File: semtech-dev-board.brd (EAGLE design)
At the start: 74 x 66 mm, 73 parts, among them Q1 BSS123, U1 MIC5219 3.3V, U2 QUALCOMM-TDK_B3710, U3 QUALCOMM-TDK_B3588, U4 SEMTECH_SX1236, Y1 32MHz

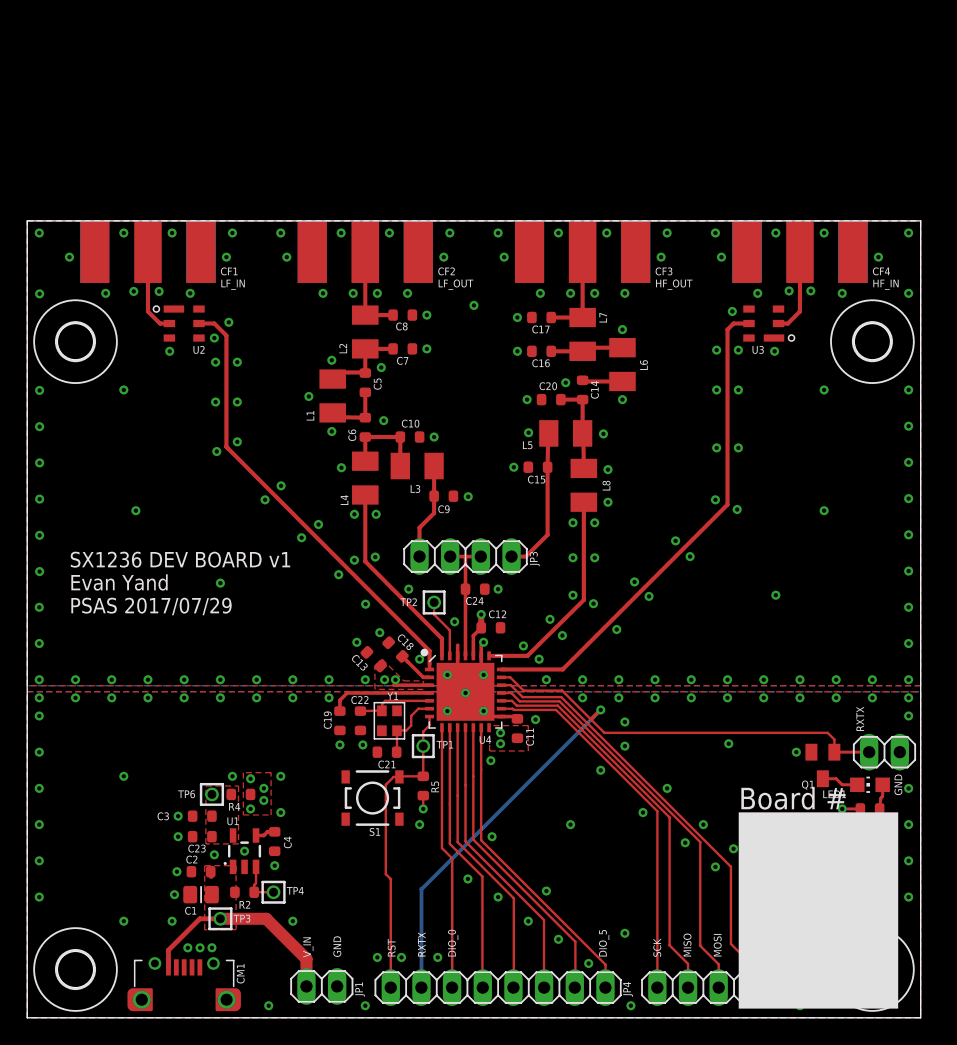
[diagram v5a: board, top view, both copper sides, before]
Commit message: Chose parts and added Digikey part numbers to BoM, switched inductors to 0603 because it was easy, shrunk board by 3 mm, cleaned up stapling, switched LEDs to 0603, oh and added a power LED for fun.
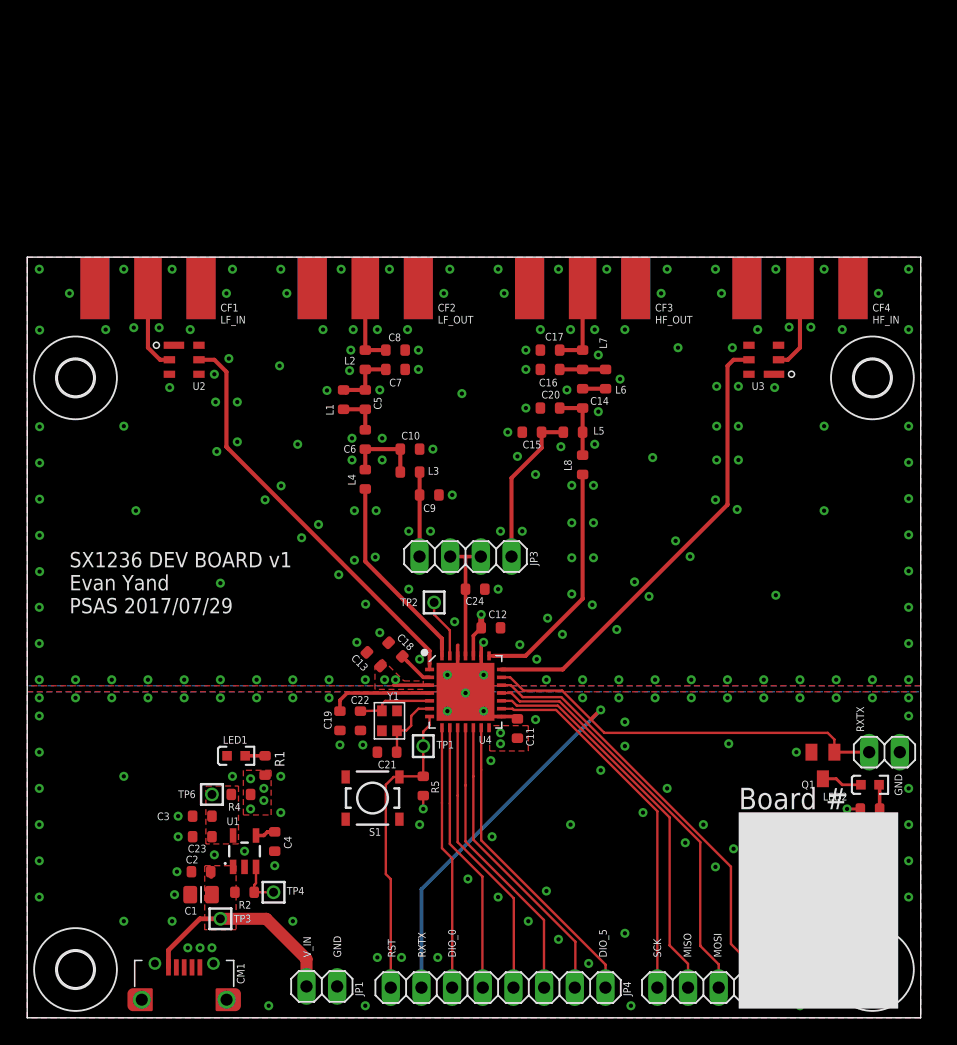
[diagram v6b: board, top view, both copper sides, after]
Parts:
- added LED2: AMB, low-gain-radio:LED-0603
- added R1: 1k, rcl_custom:.0603-B-NOSILK
- CM1: value (none) -> ZX62D-B-5P8(30)
- L1, L2, L3, L4, L5, L6, L7, L8: device rcl:L3225M -> rcl_custom:.0603-B-NOSILK
- LED1: value (none) -> GRN; device led:CHIP-LED0805 -> low-gain-radio:LED-0603
- Q1: value BSS123 -> DMN62D0U-13
- R2, R5: value 1k -> 10k
- S1: value SWITCH-MOMENTARY-2SMD-2 -> FSM4JSMATR
- moved LED1 52.6 mm to (17.3, 21.7), turned to 0 degrees
- moved CF1 3.00 mm to (10.0, 60.4)
- moved CF2 3.00 mm to (28.0, 60.4)
- moved CF3 3.00 mm to (46.0, 60.4)
- moved CF4 3.00 mm to (64.0, 60.4)
- moved U$12 3.00 mm to (72.0, 46.0)
- moved U$3 3.00 mm to (2.00, 46.0)
- moved U$8 3.00 mm to (4.00, 53.0)
- moved U$9 3.00 mm to (70.0, 53.0)
- moved U2 3.00 mm to (13.0, 54.5)
- moved U3 3.00 mm to (61.0, 54.5)
- moved C8 2.96 mm to (30.5, 55.3)
- moved C15 2.94 mm to (41.8, 48.5)
- moved C17 2.79 mm to (43.3, 55.3)
- moved L2 2.30 mm to (28.0, 54.5)
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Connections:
- new net N$5: LED1.A, R1.1
- net +3V3: now also R1.2
- net GND: now also LED1.K
- net LED+: now also LED2.A; no longer LED1.A
- net LED-: now also LED2.K; no longer LED1.C
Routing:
- net RFI_LF: track 37.5 -> 34.5 mm
- net RFI_HF: track 40.9 -> 37.9 mm
- net RFO_HF_2: track 6.02 -> 3.80 mm
- net RFO_HF: track 17.9 -> 20.0 mm
- net RFO_LF_2: track 7.26 -> 5.37 mm
- net RFO_HF_PA: track 7.66 -> 5.80 mm
- net N$5: track 0.00 -> 1.65 mm
- net RFO_LF_1: track 4.98 -> 3.50 mm
- net RFO_HF_1: track 3.32 -> 1.90 mm
- net LFO_PA_HEAD: track 8.08 -> 7.00 mm
- net RFO_HF_OUT: track 8.00 -> 7.00 mm
- net HFO_PA_HEAD: track 12.3 -> 13.1 mm
- net RFO_LF_PA: track 7.30 -> 6.50 mm
- net RFO_LF_OUT: track 7.50 -> 6.80 mm
- net RFO_LF: track 15.9 -> 16.4 mm
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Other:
- board size 74 x 66 mm -> 74 x 63 mm
